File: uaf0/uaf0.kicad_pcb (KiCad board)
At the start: 2 copper layers, 6 parts, among them X1 Клеммник_х2, X2 Клеммник_х2, X3 Клеммник_х2, X4 Клеммник_х2, X5 Клеммник_х2

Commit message: схема+трассировка, требуется проверка
не установлена ссылка на инстаграм
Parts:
- added C1: Конденсатор_керамический, N_RLC:Конденсатор_SMD_0603, B.Cu at (63.0, 83.0)
- added C10: Конденсатор_керамический, N_RLC:Конденсатор_SMD_0603, B.Cu at (82.2, 85.2)
- added C11: Конденсатор_керамический, N_RLC:Конденсатор_SMD_0603, B.Cu at (52.8, 68.0)
- added C12: Конденсатор_керамический, N_RLC:Конденсатор_SMD_0603, B.Cu at (52.8, 73.0)
- added C2: Конденсатор_керамический, N_RLC:Конденсатор_SMD_0603, B.Cu at (65.2, 83.0)
- added C3: Конденсатор_керамический, N_RLC:Конденсатор_SMD_0603, B.Cu at (84.8, 48.5)
- added C4: Конденсатор_керамический, N_RLC:Конденсатор_SMD_0603, B.Cu at (62.2, 49.0)
- added C5: Конденсатор_керамический, N_RLC:Конденсатор_SMD_0603, B.Cu at (60.0, 49.0)
- added C6: Конденсатор_керамический, N_RLC:Конденсатор_SMD_0603, B.Cu at (64.5, 49.0)
- added C7: Конденсатор_керамический, N_RLC:Конденсатор_SMD_0603, B.Cu at (68.5, 49.0)
- added C8: Конденсатор_керамический, N_RLC:Конденсатор_SMD_0603, B.Cu at (64.0, 91.0)
- added C9: Конденсатор_керамический, N_RLC:Конденсатор_SMD_0603, B.Cu at (82.2, 93.0)
- added DD2: 5559ИН10_28(UART-RS485), N_DD:SO-8, F.Cu at (79.8, 47.4)
- added FU1: Предохранитель_0.1A, N_RLC:Предохранитель_SMD_1812, F.Cu at (59.5, 56.0)
- added G***: LOGO, N_ICO:instagram_3x3, F.Cu at (71.0, 58.2)
- added G***: LOGO, N_ICO:el-nikitos_29x10, F.Cu at (77.0, 65.2)
- added G1: стабилизатор_нерегулируемый_LM1117GS-5.0, N_VD_HL:Транзистор_NPN_SOT223, F.Cu at (60.0, 47.2)
- added G2: стабилизатор_нерегулируемый_XC6206P302MR, N_VD_HL:Транзистор_IRLML6344TR_SOT-23, F.Cu at (66.8, 46.0)
- added HL1: Светодиод, N_VD_HL:Светодиод_SMD_0603, F.Cu at (65.8, 52.2)
- added HL2: Светодиод, N_VD_HL:Светодиод_SMD_0603, F.Cu at (74.2, 88.8)
- added R1: Резистор_0,065Вт, N_RLC:Резистор_SMD_0603_0,065_Вт, B.Cu at (85.2, 61.0)
- added R10: Резистор_0,065Вт, N_RLC:Резистор_SMD_0603_0,065_Вт, B.Cu at (50.5, 89.8)
- added R11: Резистор_0,065Вт, N_RLC:Резистор_SMD_0603_0,065_Вт, B.Cu at (54.0, 84.5)
- added R12: Резистор_0,065Вт, N_RLC:Резистор_SMD_0603_0,065_Вт, B.Cu at (75.8, 81.8)
- added R13: Резистор_0,065Вт, N_RLC:Резистор_SMD_0603_0,065_Вт, B.Cu at (75.8, 77.0)
- added R14: Резистор_0,065Вт, N_RLC:Резистор_SMD_0603_0,065_Вт, B.Cu at (75.8, 84.0)
- added R15: Резистор_0,065Вт, N_RLC:Резистор_SMD_0603_0,065_Вт, B.Cu at (75.8, 79.2)
- added R16: Резистор_0,065Вт, N_RLC:Резистор_SMD_0603_0,065_Вт, B.Cu at (80.5, 82.0)
- added R17: Резистор_0,065Вт, N_RLC:Резистор_SMD_0603_0,065_Вт, B.Cu at (80.5, 77.0)
- added R18: Резистор_0,065Вт, N_RLC:Резистор_SMD_0603_0,065_Вт, B.Cu at (85.2, 82.0)
- added R19: Резистор_0,065Вт, N_RLC:Резистор_SMD_0603_0,065_Вт, B.Cu at (85.2, 77.0)
- added R2: Резистор_0,065Вт, N_RLC:Резистор_SMD_0603_0,065_Вт, B.Cu at (85.2, 56.0)
- added R20: Резистор_0,065Вт, N_RLC:Резистор_SMD_0603_0,065_Вт, B.Cu at (82.2, 90.8)
- added R21: Резистор_0,065Вт, N_RLC:Резистор_SMD_0603_0,065_Вт, B.Cu at (82.2, 87.5)
- added R22: Резистор_0,065Вт, N_RLC:Резистор_SMD_0603_0,065_Вт, B.Cu at (85.2, 90.8)
- added R23: Резистор_0,065Вт, N_RLC:Резистор_SMD_0603_0,065_Вт, B.Cu at (85.2, 87.5)
- added R24: Резистор_0,065Вт, N_RLC:Резистор_SMD_0603_0,065_Вт, B.Cu at (64.2, 70.2)
- added R25: Резистор_0,065Вт, N_RLC:Резистор_SMD_0603_0,065_Вт, B.Cu at (64.2, 75.2)
- added R26: Резистор_0,065Вт, N_RLC:Резистор_SMD_0603_0,065_Вт, B.Cu at (61.8, 65.2)
- added R27: Резистор_0,065Вт, N_RLC:Резистор_SMD_0603_0,065_Вт, B.Cu at (61.8, 70.2)
- added R28: Резистор_0,065Вт, N_RLC:Резистор_SMD_0603_0,065_Вт, B.Cu at (61.8, 75.2)
- added R3: Резистор_0,065Вт, N_RLC:Резистор_SMD_0603_0,065_Вт, B.Cu at (74.2, 45.2)
- added R4: Резистор_0,065Вт, N_RLC:Резистор_SMD_0603_0,065_Вт, B.Cu at (68.5, 51.8)
- added R5: Резистор_0,065Вт, N_RLC:Резистор_SMD_0603_0,065_Вт, B.Cu at (72.5, 88.5)
- added R6: Резистор_0,065Вт, N_RLC:Резистор_SMD_0603_0,065_Вт, B.Cu at (74.2, 49.8)
- added R7: Резистор_0,065Вт, N_RLC:Резистор_SMD_0603_0,065_Вт, B.Cu at (74.2, 47.5)
- added R8: Резистор_0,065Вт, N_RLC:Резистор_SMD_0603_0,065_Вт, B.Cu at (55.8, 79.2)
- added R9: Резистор_0,065Вт, N_RLC:Резистор_SMD_0603_0,065_Вт, B.Cu at (48.0, 89.8)
- added VD1: Диод_шоттки_S13, N_VD_HL:Диод_S13_SOD-123, B.Cu at (55.5, 81.8)
- added VT1: Транзистор_полевой_N-IRLML6344TR, N_VD_HL:Транзистор_IRLML6344TR_SOT-23, F.Cu at (81.5, 81.8)
- added VT2: Транзистор_полевой_N-IRLML6344TR, N_VD_HL:Транзистор_IRLML6344TR_SOT-23, F.Cu at (81.5, 76.8)
- added VT3: Транзистор_полевой_N-IRLML6344TR, N_VD_HL:Транзистор_IRLML6344TR_SOT-23, F.Cu at (57.8, 67.0)
- added VT4: Транзистор_полевой_N-IRLML6344TR, N_VD_HL:Транзистор_IRLML6344TR_SOT-23, F.Cu at (57.8, 72.0)
- added X6: Клеммник_х2, N_X:Клеммник_х2_шаг5, F.Cu at (90.0, 61.0)
- added X7: Клеммник_х2, N_X:Клеммник_х2_шаг5, F.Cu at (90.0, 51.0)
- added X8: Клеммник_х2, N_X:Клеммник_х2_шаг5, F.Cu at (90.0, 72.0)
- added XP1: Вилка_PLD6_ПРОГ, N_X:Вилка_PLD6_вертикальная, F.Cu at (48.0, 79.2)
- moved X2 82.6 mm to (50.0, 56.0), turned to 270 degrees
- moved X1 71.8 mm to (50.0, 46.0), turned to 270 degrees
- moved X3 70.2 mm to (50.0, 67.0), turned to 270 degrees
- moved X5 45.4 mm to (90.0, 92.0), turned to 90 degrees
- moved DD1 38.8 mm to (67.2, 82.2), turned to 270 degrees
- moved X4 29.9 mm to (90.0, 82.0), turned to 90 degrees
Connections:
- DD1 pad 1: Net-(DD1-Pad1) -> /PD3_INT1
- DD1 pad 12: Net-(DD1-Pad12) -> /PB0
- DD1 pad 13: Net-(DD1-Pad13) -> /PB1_OC1A
- DD1 pad 14: Net-(DD1-Pad14) -> /PB2_OC1B
- DD1 pad 15: Net-(DD1-Pad15) -> /MOSI
- DD1 pad 16: Net-(DD1-Pad16) -> /MISO
- DD1 pad 17: Net-(DD1-Pad17) -> /SCK
- DD1 pad 18: Net-(DD1-Pad18) -> /5V
- DD1 pad 20: Net-(DD1-Pad20) -> /3V
- DD1 pad 21: Net-(DD1-Pad21) -> /GND
- DD1 pad 23: Net-(DD1-Pad23) -> /PC0
- DD1 pad 24: Net-(DD1-Pad24) -> /PC1
- DD1 pad 26: Net-(DD1-Pad26) -> /PC3
- DD1 pad 27: Net-(DD1-Pad27) -> /SDA
- DD1 pad 28: Net-(DD1-Pad28) -> /SCL
- DD1 pad 29: Net-(DD1-Pad29) -> /RES
- DD1 pad 3: Net-(DD1-Pad3) -> /GND
- DD1 pad 30: Net-(DD1-Pad30) -> /RX
- DD1 pad 31: Net-(DD1-Pad31) -> /TX
- DD1 pad 32: Net-(DD1-Pad32) -> /PD2_INT0
- DD1 pad 4: Net-(DD1-Pad4) -> /5V
- DD1 pad 5: Net-(DD1-Pad5) -> /GND
- DD1 pad 6: Net-(DD1-Pad6) -> /5V
- X2 pad 1: /GND -> /PWR_GND
- X2 pad 2: /GND -> /PWR_GND
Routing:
- net /3V: track 0.00 -> 104.3 mm, vias 0 -> 3
- net /TX: track 0.00 -> 96.5 mm, vias 0 -> 1
- net /RX: track 0.00 -> 92.1 mm, vias 0 -> 1
- net /PWR_GND: track 0.00 -> 80.1 mm, vias 0 -> 2
- net /5V: track 0.00 -> 68.6 mm, vias 0 -> 11
- net /SCL: track 0.00 -> 61.6 mm, vias 0 -> 2
- net /SDA: track 0.00 -> 56.5 mm, vias 0 -> 2
- net /PB0: track 0.00 -> 53.8 mm, vias 0 -> 1
- net /GND: track 0.00 -> 32.2 mm, vias 0 -> 10
- net /RES: track 0.00 -> 30.6 mm, vias 0 -> 1
- net /PC0: track 0.00 -> 26.9 mm, vias 0 -> 1
- net /PC1: track 0.00 -> 25.7 mm, vias 0 -> 1
- net /12V: track 0.00 -> 24.3 mm, vias 0 -> 1
- net /PB1_OC1A: track 0.00 -> 23.9 mm, vias 0 -> 1
- net /PB2_OC1B: track 0.00 -> 18.8 mm, vias 0 -> 1
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- added copper zone on F.Cu, net /5V
- added copper zone on B.Cu, net /GND
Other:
- board outline added: 50 x 52.5 mm
- net class PWR added: clearance 0.4, trace_width 0.45, via_dia 0.8, via_drill 0.4
- board text added: "12V"
- board text added: "AI_1"
- board text added: "AI_2"
- board text added: "DI_1"
- board text added: "DI_2"
- board text added: "DO_1"
- board text added: "DO_2"
- board text added: "GND"
- board text added: "PWR_GND"
- board text added: "RS_A"
- board text added: "RS_B"
- board text added: "SCL"
- board text added: "SDA"
- board text added: "uaf.0(10/19)"

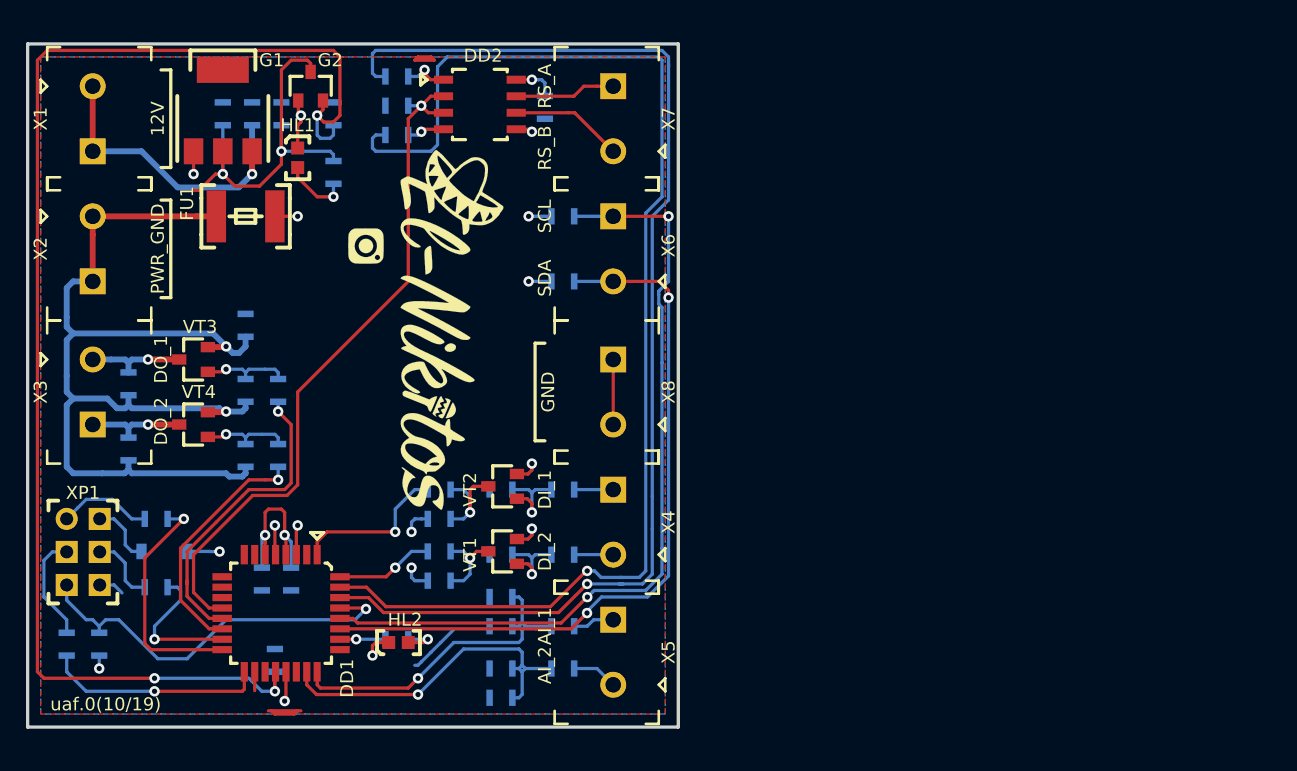
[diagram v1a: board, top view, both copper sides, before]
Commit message: исправлена шелкография, добавлены файлы производства v0
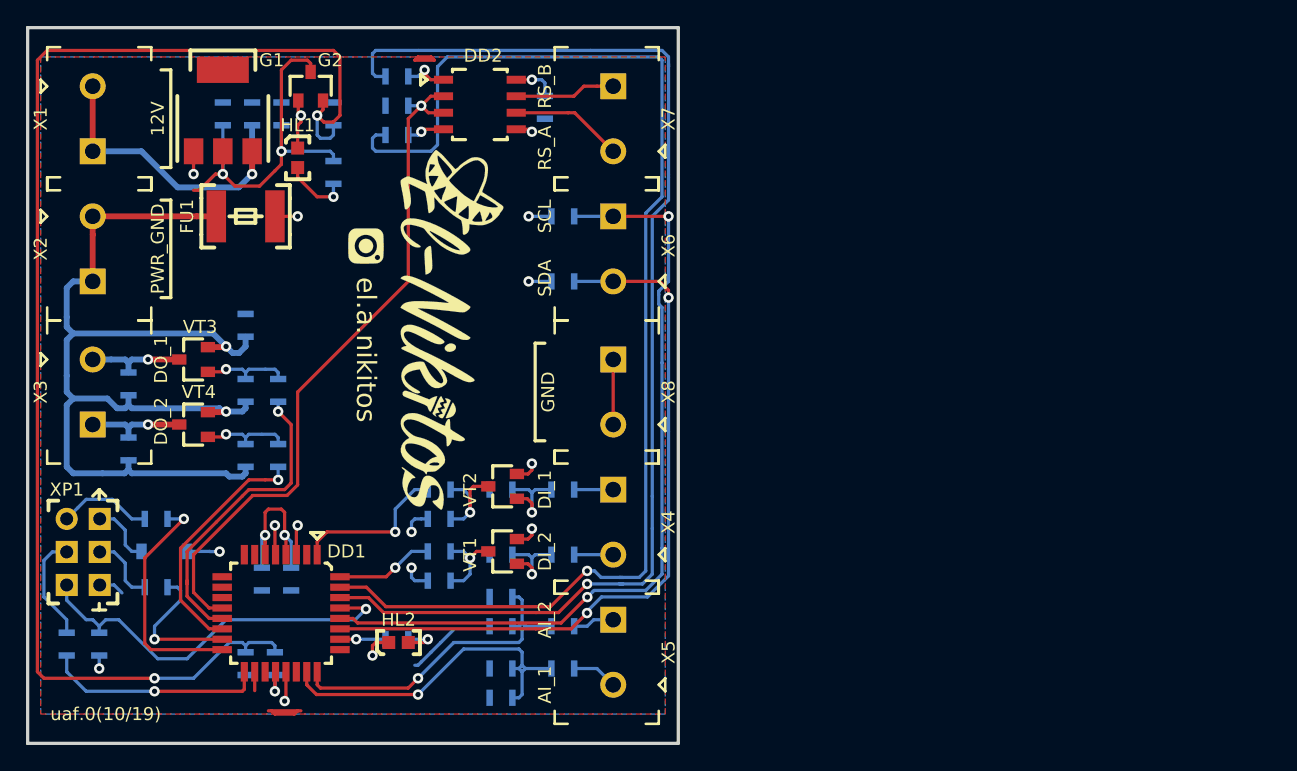
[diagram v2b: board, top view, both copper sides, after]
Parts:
- added R29: Резистор_0,065Вт, N_RLC:Резистор_SMD_0603_0,065_Вт, B.Cu at (64.0, 91.2)
- moved C8 2.70 mm to (61.8, 89.5), turned to 270 degrees
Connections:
- DD1 pad 20: /3V -> Net-(DD1-Pad20)
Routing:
- net Net-(DD1-Pad20): track 0.00 -> 2.75 mm, vias 0 -> 1
- net /3V: track 104.3 -> 103.4 mm, vias 3 -> 2
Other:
- board size 50 x 52.5 mm -> 50 x 55 mm
- board text added: "el.a.nikitos"

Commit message: скетч для генератора "колоколов"
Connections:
- R18 pad 2: /DI_1 -> /DI_2
- R19 pad 2: /DI_2 -> /DI_1
- X4 pad 1: /DI_1 -> /DI_2
- X4 pad 2: /DI_2 -> /DI_1
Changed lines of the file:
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@@
     (fp_line (start 8 3.5) (end 8 2.5) (layer F.SilkS) (width 0.2))
     (pad 2 thru_hole rect (at 5 0 90) (size 2 2) (drill 1.2) (layers *.Cu *.Mask)
+      (net 15 /DI_1))
+    (pad 1 thru_hole circle (at 0 0 90) (size 2 2) (drill 1.2) (layers *.Cu *.Mask)
       (net 14 /DI_2))
-    (pad 1 thru_hole circle (at 0 0 90) (size 2 2) (drill 1.2) (layers *.Cu *.Mask)
-      (net 15 /DI_1))
     (model ${N_3D}/XT_DG301-5_0-2P12.STEP
       (at (xyz 0 0 0))
@@
     (fp_line (start -0.5 0.9) (end 0 0.9) (layer B.SilkS) (width 0.25))
     (pad 2 smd rect (at 1.75 0) (size 0.5 1.25) (layers B.Cu B.Paste B.Mask)
-      (net 14 /DI_2) (clearance 0.2))
+      (net 15 /DI_1) (clearance 0.2))
     (pad 1 smd rect (at 0 0) (size 0.5 1.25) (layers B.Cu B.Paste B.Mask)
       (net 48 "Net-(R17-Pad2)") (clearance 0.2))
@@
     (fp_line (start -0.5 0.9) (end 0 0.9) (layer B.SilkS) (width 0.25))
     (pad 2 smd rect (at 1.75 0) (size 0.5 1.25) (layers B.Cu B.Paste B.Mask)
-      (net 15 /DI_1) (clearance 0.2))
+      (net 14 /DI_2) (clearance 0.2))
     (pad 1 smd rect (at 0 0) (size 0.5 1.25) (layers B.Cu B.Paste B.Mask)
       (net 47 "Net-(R16-Pad2)") (clearance 0.2))
@@
   (segment (start 53 67) (end 54.25 67) (width 0.45) (layer B.Cu) (net 13))
   (segment (start 54.25 67) (end 56.5 67) (width 0.45) (layer F.Cu) (net 13))
-  (segment (start 87 77) (end 90 77) (width 0.25) (layer B.Cu) (net 14))
-  (segment (start 87 82) (end 90 82) (width 0.25) (layer B.Cu) (net 15))
+  (segment (start 87 77) (end 90 77) (width 0.25) (layer B.Cu) (net 15))
+  (segment (start 87 82) (end 90 82) (width 0.25) (layer B.Cu) (net 14) (status 1000000))
   (segment (start 88 87.5) (end 88.5 87) (width 0.25) (layer B.Cu) (net 16))
   (segment (start 87 87.5) (end 88 87.5) (width 0.25) (layer B.Cu) (net 16))
@@
   (segment (start 68.25 50) (end 68.5 49.75) (width 0.25) (layer B.Cu) (net 19))
   (segment (start 68.5 49.75) (end 68.5 49) (width 0.25) (layer B.Cu) (net 19))
-  (segment (start 64 92.5) (end 64 91) (width 0.25) (layer F.Cu) (net 53))
   (via (at 54.75 91.5) (size 0.8) (drill 0.4) (layers F.Cu B.Cu) (net 19))
   (segment (start 68.5 48.75) (end 67.75 48.75) (width 0.25) (layer F.Cu) (net 19))
@@
   (segment (start 69 88.5) (end 70.25 88.5) (width 0.25) (layer F.Cu) (net 52))
   (segment (start 70.25 88.5) (end 72.5 88.5) (width 0.25) (layer B.Cu) (net 52))
+  (segment (start 64 92.5) (end 64 91) (width 0.25) (layer F.Cu) (net 53))
   (via (at 64 92.5) (size 0.8) (drill 0.4) (layers F.Cu B.Cu) (net 53))
   (segment (start 64 91.25) (end 64 92.5) (width 0.25) (layer B.Cu) (net 53))
